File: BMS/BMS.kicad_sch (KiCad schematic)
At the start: 0 parts

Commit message: Added symbols, models, footprints for BMS and added wiring for Safety and the Brain
Original-author: Zachariah K. Sharma <zachariah.sharma@gmail.com>
Source-commit: 61d43b963560d7d84e99585d61830151d00a31d1
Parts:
- added C1: 100nF, PCM_JLCPCB:C_0402, symbol PCM_JLCPCB-Capacitors:0402,100nF
- added C2: 10uF, PCM_JLCPCB:C_0603, symbol PCM_JLCPCB-Capacitors:0603,10uF
- added C3, C4: 1uF, PCM_JLCPCB:C_0402, symbol PCM_JLCPCB-Capacitors:0402,1uF
- added J1: USB4105-GF-A, USB4105-GF-A:GCT_USB4105-GF-A, symbol USB4105-GF-A:USB4105-GF-A
- added R1: 330Ω, PCM_JLCPCB:R_0402, symbol PCM_JLCPCB-Resistors:0402,330Ω
- added R2: 2.2kΩ, PCM_JLCPCB:R_0402, symbol PCM_JLCPCB-Resistors:0402,2.2kΩ
- added RT1: NCP15XH103F03RC, NCP15XH103F03RC:THRMC1005X55N, symbol NCP15XH103F03RC:NCP15XH103F03RC
- added U1: BQ29700DSER, BQ29700DSER:SON50P150X150X80-6N, symbol BQ29700DSER:BQ29700DSER
- added U2: BQ25180YBGR, BQ25180YBGR:IC_BQ25180YBGR, symbol BQ25180YBGR:BQ25180YBGR
- added U3, U5: CSD16406Q3, CSD16406Q3:TRANS_CSD16406Q3, symbol CSD16406Q3:CSD16406Q3
- added U4: TPD2E2U06DCKR, TPD2E2U06DCKR:SOT65P210X110-3N, symbol TPD2E2U06DCKR:TPD2E2U06DCKR
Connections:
- new net: C2.1, U2.B2 (SYS)
- new net: RT1.1, U2.D1 (TS/MR)
- new net: C1.2, R1.2, U1.5 (BAT)
- new net: R2.2, U1.6 (V-)
- new net CELL+: R1.1
- new net CELL-: C1.1, U1.4 (VSS), U5.1, U5.2, U5.3
- new net COUT: U1.2 (COUT), U3.4
- new net DOUT: U1.3 (DOUT), U5.4
- new net FET_MID: U3.5, U3.6, U3.7, U3.8, U5.5, U5.6, U5.7, U5.8
- new net GND: C2.2, C3.1, C4.1, J1.A1_B12 (GND), J1.B1_A12 (GND), RT1.2, U2.D2 (GND)
- new net PACK-: R2.1, U3.1, U3.2, U3.3
- new net PACK_P: C4.2, U2.C2 (BAT)
- new net SHELL_GND: J1.SH1 (SHELL_GND), J1.SH2 (SHELL_GND), J1.SH3 (SHELL_GND), J1.SH4 (SHELL_GND)
- new net VBUS: C3.2, J1.A4_B9 (VBUS), J1.B4_A9 (VBUS), U2.A2 (IN)
- no-connect marks 0 -> 3
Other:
- note added: "Brain"
- note added: "Charge"
- note added: "Discharge"
- note added: "Safety"
- note added: "USB"

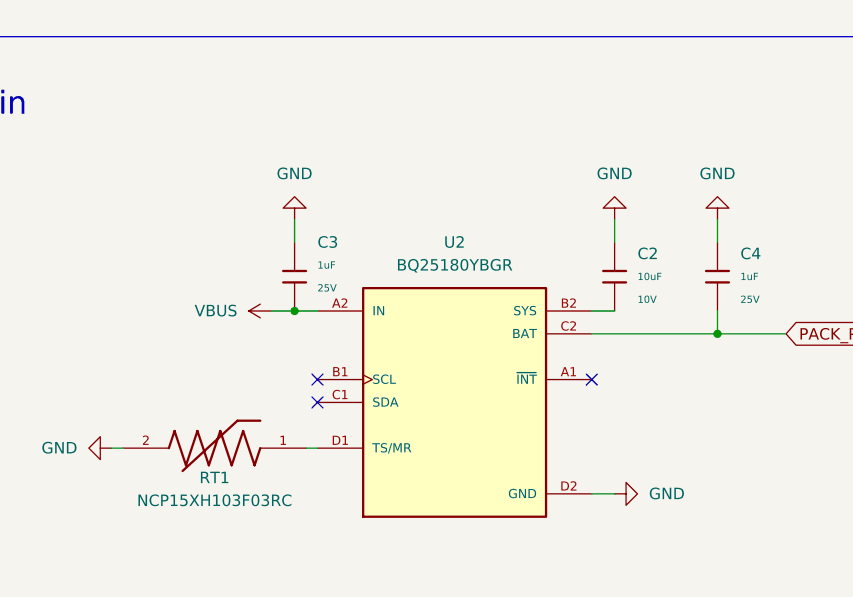
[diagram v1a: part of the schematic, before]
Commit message: Finished wiring for Brain, changed to 4 leafs without EN because we're using 1S4P config
Original-author: Zachariah K. Sharma <zachariah.sharma@gmail.com>
Source-commit: d838f67f28fdc3c8cd17522192b40c13826d0008
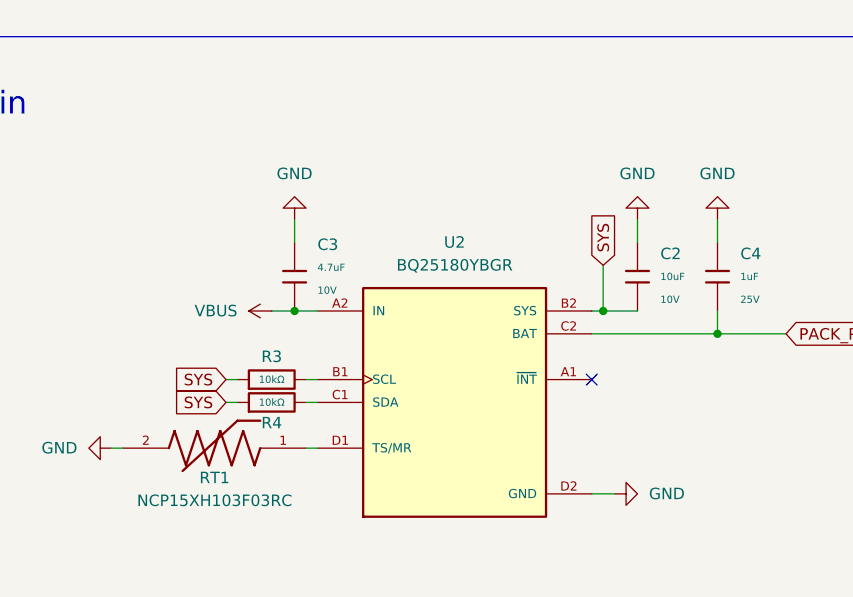
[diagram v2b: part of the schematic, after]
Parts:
- removed C3: 1uF, PCM_JLCPCB:C_0402, symbol PCM_JLCPCB-Capacitors:0402,1uF
- added C3: 4.7uF, PCM_JLCPCB:C_0402, symbol PCM_JLCPCB-Capacitors:0402,4.7uF
- added R3, R4: 10kΩ, PCM_JLCPCB:R_0402, symbol PCM_JLCPCB-Resistors:0402,10kΩ
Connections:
- net GND: now also C3.1
- net VBUS: now also C3.2
- net SYS: now reaches C2.1, U2.B2 (SYS)
- net SYS: now also R3.1, R4.1
- net at U2.B1 (SCL): now also R3.2
- net at U2.C1 (SDA): now also R4.2
- no-connect marks 3 -> 1
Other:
- moved on the sheet: C2
